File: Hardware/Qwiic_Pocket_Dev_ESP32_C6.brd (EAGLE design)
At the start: 25.4 x 25.4 mm, 96 parts, among them J1 USB Female Type C Connector, J4 QWIIC_RIGHT_ANGLE, Q1 20V/4.2A/52mΩ/1.4W, U1 ESP32-C6-MINI-1, U2 RT9080-33GJ5, U3 MCP73831

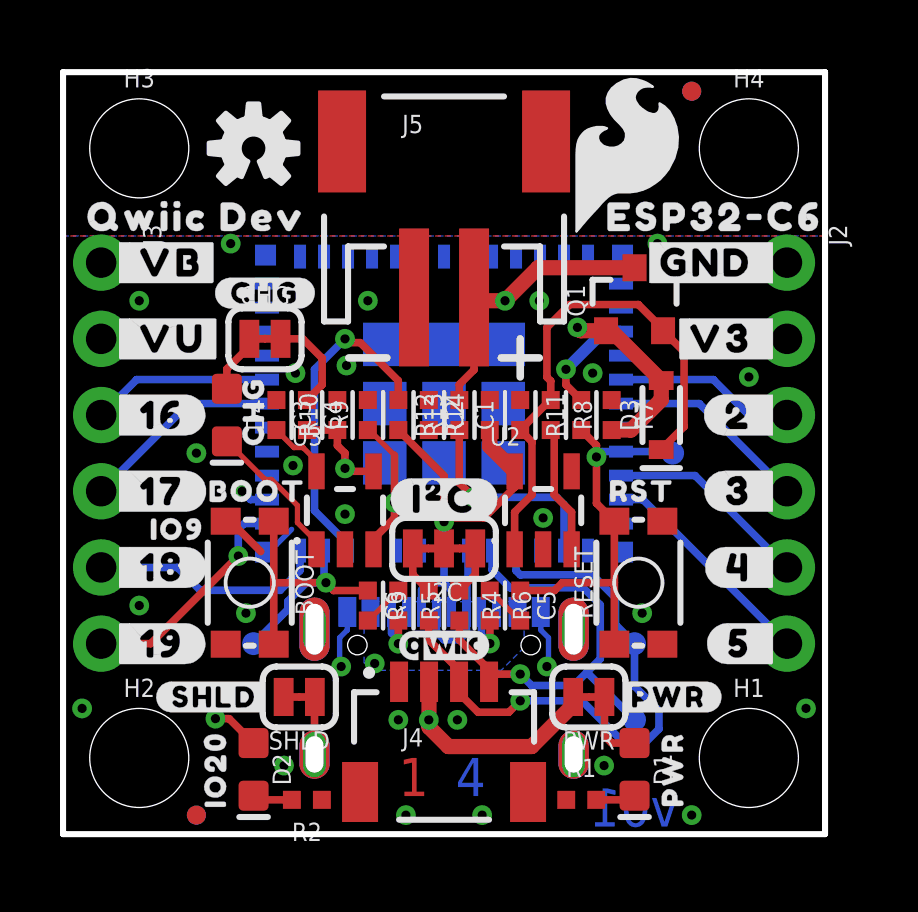
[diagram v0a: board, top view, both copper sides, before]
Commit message: Change STAT LED to GPIO23
GPIO20 likes to magically start toggling the LED when touching GPIO19. Something to do with the SDIO pins, I think
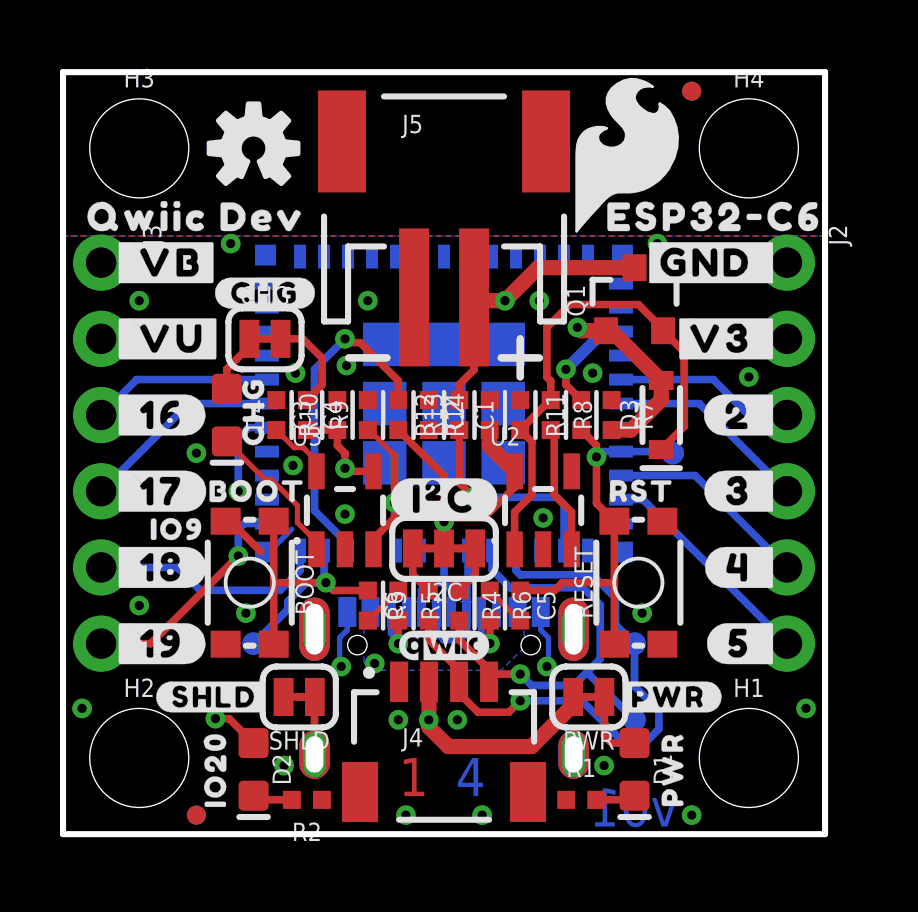
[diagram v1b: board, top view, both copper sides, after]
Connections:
- removed net IO20/STAT: D2.A, U1.26
- new net IO23/STAT: D2.A, U1.29
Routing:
- net IO23/STAT: track 0.00 -> 12.4 mm, vias 0 -> 2
- net IO20/STAT: track 10.5 -> 0.00 mm, vias 2 -> 0
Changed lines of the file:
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@@
 <drawing>
 <settings>
-<setting alwaysvectorfont="yes"/>
+<setting alwaysvectorfont="no"/>
 <setting verticaltext="up"/>
 </settings>
@@
 <wire x1="2.921" y1="6.35" x2="1.27" y2="6.35" width="0.254" layer="1"/>
 </signal>
-<signal name="IO20/STAT">
-<contactref element="U1" pad="26"/>
+<signal name="IO23/STAT">
 <contactref element="D2" pad="A"/>
-<wire x1="6.8" y1="11.151" x2="6.248" y2="11.151" width="0.254" layer="16"/>
-<wire x1="6.248" y1="11.151" x2="5.969" y2="11.43" width="0.254" layer="16"/>
-<via x="5.969" y="11.43" extent="1-16" drill="0.3048"/>
-<wire x1="5.969" y1="11.43" x2="5.08" y2="10.541" width="0.254" layer="2"/>
+<via x="5.842" y="11.43" extent="1-16" drill="0.3048"/>
+<wire x1="5.842" y1="11.43" x2="5.08" y2="10.668" width="0.254" layer="2"/>
 <via x="5.08" y="3.85" extent="1-16" drill="0.3048"/>
 <wire x1="5.536" y1="3.85" x2="6.35" y2="3.036" width="0.254" layer="1"/>
 <wire x1="5.536" y1="3.85" x2="5.08" y2="3.85" width="0.254" layer="1"/>
-<wire x1="5.08" y1="10.541" x2="5.08" y2="3.85" width="0.254" layer="2"/>
+<wire x1="5.08" y1="10.668" x2="5.08" y2="3.85" width="0.254" layer="2"/>
+<contactref element="U1" pad="29"/>
+<wire x1="5.842" y1="11.43" x2="5.842" y2="13.208" width="0.254" layer="16"/>
+<wire x1="6.185" y1="13.551" x2="6.8" y2="13.551" width="0.254" layer="16"/>
+<wire x1="5.842" y1="13.208" x2="6.185" y2="13.551" width="0.254" layer="16"/>
 </signal>
 <signal name="IO1/V_BATT_2">

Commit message: v10 updates
Bump version number
Update STAT LED IO silk label
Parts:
- removed U$4: (no value), output:IO200
- added U$28: (no value), output:IO230
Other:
- board text added: "v10"
- board text removed: "v01"
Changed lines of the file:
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@@
 <layer number="19" name="Unrouted" color="6" fill="1" visible="yes" active="yes"/>
 <layer number="20" name="Dimension" color="24" fill="1" visible="yes" active="yes"/>
-<layer number="21" name="tPlace" color="16" fill="1" visible="no" active="yes"/>
+<layer number="21" name="tPlace" color="16" fill="1" visible="yes" active="yes"/>
 <layer number="22" name="bPlace" color="14" fill="1" visible="yes" active="yes"/>
 <layer number="23" name="tOrigins" color="15" fill="1" visible="yes" active="yes"/>
@@
 <wire x1="0" y1="25.4" x2="0" y2="0" width="0.2032" layer="20"/>
 <rectangle x1="9.398" y1="8.128" x2="9.652" y2="8.382" layer="42"/>
-<text x="19.05" y="0.889" size="1.27" layer="16" font="vector" ratio="15" rot="MR0" align="center">v01</text>
+<text x="19.05" y="0.889" size="1.27" layer="16" font="vector" ratio="15" rot="MR0" align="center">v10</text>
 <wire x1="10.668" y1="6.858" x2="10.668" y2="8.382" width="0.1524" layer="21"/>
 <wire x1="11.684" y1="6.858" x2="11.684" y2="8.382" width="0.1524" layer="21"/>
@@
 <element name="FRAME1" library="SparkFun-Aesthetics" package="CREATIVE_COMMONS" value="FRAME-LETTER" x="-10.16" y="-25.4" smashed="yes">
 <attribute name="DESIGNER" value="Dryw Wade" x="-10.16" y="-25.4" size="1.778" layer="27" font="vector" ratio="15" display="off"/>
-<attribute name="REV" value="v01" x="-10.16" y="-25.4" size="1.778" layer="27" font="vector" ratio="15" display="off"/>
+<attribute name="REV" value="v10" x="-10.16" y="-25.4" size="1.778" layer="27" font="vector" ratio="15" display="off"/>
 </element>
 <element name="U$1" library="output" package="#_GND#0" value="" x="23.876" y="19.05" smashed="yes" rot="MR0"/>
@@
 <element name="U$5" library="output" package="#GND_#0" value="" x="24.003" y="19.05" smashed="yes"/>
 <element name="U$3" library="output" package="#V3_#0" value="" x="24.003" y="16.51" smashed="yes"/>
-<element name="U$4" library="output" package="IO200" value="" x="5.08" y="2.159" smashed="yes" rot="R90"/>
 <element name="LOGO1" library="SparkFun-Aesthetics" package="BLANK" value="SFE_LOGO_NAME_FLAMEBLANK" x="-8.89" y="-25.4" smashed="yes"/>
 <element name="LOGO2" library="SparkFun-Aesthetics" package="OSHW-LOGO-S" value="OSHW-LOGOS" x="6.35" y="22.86" smashed="yes"/>
@@
 <attribute name="VALUE" x="11.63" y="13.97" size="0.6096" layer="27" font="vector" ratio="20" rot="R270" align="top-center"/>
 </element>
+<element name="U$28" library="output" package="IO230" value="" x="5.08" y="2.159" smashed="yes" rot="R90"/>
 </elements>
 <signals>
